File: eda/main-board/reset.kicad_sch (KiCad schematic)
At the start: 8 parts, among them U10 74HCT00, U2 NA555P

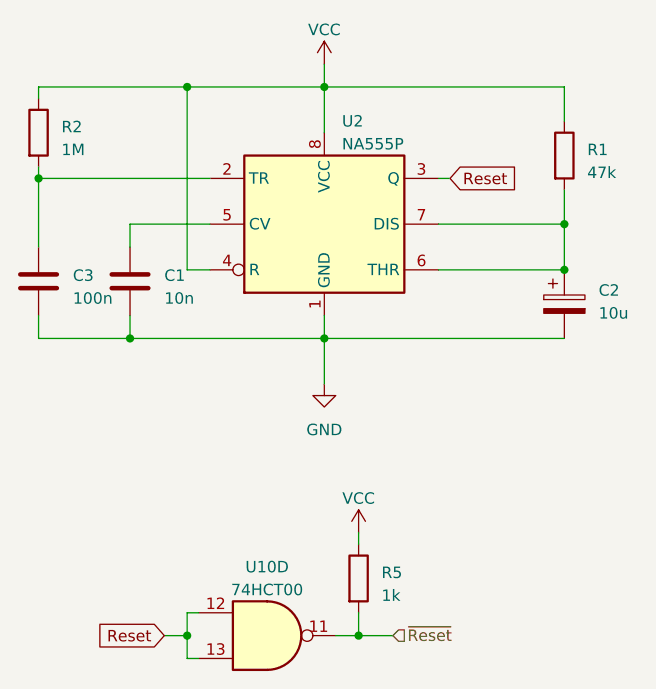
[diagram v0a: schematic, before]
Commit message: EDA work for new expansion header
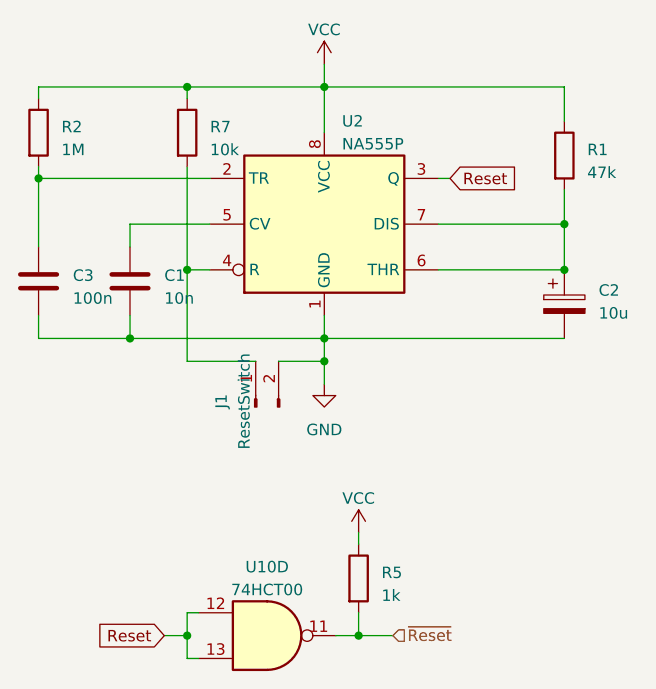
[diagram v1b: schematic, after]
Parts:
- added J1: ResetSwitch, Connector_PinHeader_2.54mm:PinHeader_1x02_P2.54mm_Vertical, symbol Connector:Conn_01x02_Pin
- added R7: 10k, Resistor_THT:R_Axial_DIN0207_L6.3mm_D2.5mm_P7.62mm_Horizontal, symbol Device:R
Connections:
- net GND: now also J1.2 (Pin_2)
- net VCC: now also R7.1; no longer U2.4 (R)
- new net: J1.1 (Pin_1), R7.2, U2.4 (R)
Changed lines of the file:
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@@
   (junction (at 129.54 69.85) (diameter 0) (color 0 0 0 0)
   )
+  (junction (at 102.87 80.01) (diameter 0) (color 0 0 0 0)
+  )
   (junction (at 102.87 77.47) (diameter 0) (color 0 0 0 0)
   )
@@
   (junction (at 87.63 110.49) (diameter 0) (color 0 0 0 0)
   )
+  (junction (at 87.63 69.85) (diameter 0) (color 0 0 0 0)
+  )
   (junction (at 71.12 59.69) (diameter 0) (color 0 0 0 0)
   )
+  (wire (pts (xy 102.87 82.55) (xy 102.87 80.01))
+    (stroke (width 0) (type default))
+  )
+  (wire (pts (xy 87.63 49.53) (xy 87.63 50.8))
+    (stroke (width 0) (type default))
+  )
+  (wire (pts (xy 81.28 77.47) (xy 102.87 77.47))
+    (stroke (width 0) (type default))
+  )
+  (wire (pts (xy 71.12 74.93) (xy 71.12 77.47))
+    (stroke (width 0) (type default))
+  )
+  (wire (pts (xy 106.68 110.49) (xy 110.49 110.49))
+    (stroke (width 0) (type default))
+  )
+  (wire (pts (xy 81.28 74.93) (xy 81.28 77.47))
+    (stroke (width 0) (type default))
+  )
+  (wire (pts (xy 71.12 77.47) (xy 81.28 77.47))
+    (stroke (width 0) (type default))
+  )
+  (wire (pts (xy 102.87 46.99) (xy 102.87 49.53))
+    (stroke (width 0) (type default))
+  )
   (wire (pts (xy 87.63 49.53) (xy 102.87 49.53))
     (stroke (width 0) (type default))
   )
-  (wire (pts (xy 102.87 82.55) (xy 102.87 77.47))
-    (stroke (width 0) (type default))
-  )
-  (wire (pts (xy 81.28 77.47) (xy 102.87 77.47))
-    (stroke (width 0) (type default))
-  )
-  (wire (pts (xy 71.12 74.93) (xy 71.12 77.47))
-    (stroke (width 0) (type default))
-  )
-  (wire (pts (xy 106.68 110.49) (xy 110.49 110.49))
-    (stroke (width 0) (type default))
-  )
-  (wire (pts (xy 81.28 74.93) (xy 81.28 77.47))
-    (stroke (width 0) (type default))
-  )
-  (wire (pts (xy 71.12 77.47) (xy 81.28 77.47))
-    (stroke (width 0) (type default))
-  )
-  (wire (pts (xy 102.87 46.99) (xy 102.87 49.53))
-    (stroke (width 0) (type default))
-  )
   (wire (pts (xy 88.9 107.95) (xy 87.63 107.95))
     (stroke (width 0) (type default))
@@
     (stroke (width 0) (type default))
   )
+  (wire (pts (xy 87.63 69.85) (xy 87.63 80.01))
+    (stroke (width 0) (type default))
+  )
   (wire (pts (xy 87.63 110.49) (xy 87.63 113.03))
     (stroke (width 0) (type default))
@@
     (stroke (width 0) (type default))
   )
+  (wire (pts (xy 87.63 58.42) (xy 87.63 69.85))
+    (stroke (width 0) (type default))
+  )
   (wire (pts (xy 129.54 64.77) (xy 115.57 64.77))
     (stroke (width 0) (type default))
@@
     (stroke (width 0) (type default))
   )
-  (wire (pts (xy 87.63 69.85) (xy 87.63 49.53))
+  (wire (pts (xy 87.63 80.01) (xy 95.25 80.01))
     (stroke (width 0) (type default))
   )
@@
     (stroke (width 0) (type default))
   )
+  (wire (pts (xy 97.79 80.01) (xy 102.87 80.01))
+    (stroke (width 0) (type default))
+  )
   (wire (pts (xy 90.17 69.85) (xy 87.63 69.85))
     (stroke (width 0) (type default))
   )
   (wire (pts (xy 81.28 67.31) (xy 81.28 64.77))
+    (stroke (width 0) (type default))
+  )
+  (wire (pts (xy 102.87 80.01) (xy 102.87 77.47))
     (stroke (width 0) (type default))
   )
@@
     )
   )
+  (symbol (lib_id "Connector:Conn_01x02_Pin") (at 95.25 85.09 90) (unit 1)
+    (in_bom yes) (on_board yes) (dnp no)
+    (property "Reference" "J1" (at 91.44 84.455 0)
+      (effects (font (size 1.27 1.27)))
+    )
+    (property "Value" "ResetSwitch" (at 93.98 84.455 0)
+      (effects (font (size 1.27 1.27)))
+    )
+    (property "Footprint" "Connector_PinHeader_2.54mm:PinHeader_1x02_P2.54mm_Vertical" (at 95.25 85.09 0)
+      (effects (font (size 1.27 1.27)) hide)
+    )
+    (property "Datasheet" "~" (at 95.25 85.09 0)
+      (effects (font (size 1.27 1.27)) hide)
+    )
+    (pin "1")
+    (pin "2")
+    (instances
+      (project "main-board"
+        (path "/2957ffac-6a43-4af7-8ab7-5cc1dbf2f2d7"
+          (reference "J1") (unit 1)
+        )
+        (path "/2957ffac-6a43-4af7-8ab7-5cc1dbf2f2d7/9790c182-812b-4e14-896c-2d1a7e725d4e"
+          (reference "J1") (unit 1)
+        )
+        (path "/2957ffac-6a43-4af7-8ab7-5cc1dbf2f2d7/9b235015-96d2-4548-9fc4-8bf7ce4b5d0e"
+          (reference "J3") (unit 1)
+        )
+      )
+    )
+  )
   (symbol (lib_id "Device:R") (at 71.12 54.61 0) (unit 1)
     (in_bom yes) (on_board yes) (dnp no) (fields_autoplaced)
@@
         )
       )
+    )
+  )
+  (symbol (lib_id "Device:R") (at 87.63 54.61 0) (unit 1)
+    (in_bom yes) (on_board yes) (dnp no) (fields_autoplaced)
+    (property "Reference" "R7" (at 90.17 53.975 0)
+      (effects (font (size 1.27 1.27)) (justify left))
+    )
+    (property "Value" "10k" (at 90.17 56.515 0)
+      (effects (font (size 1.27 1.27)) (justify left))
+    )
+    (property "Footprint" "Resistor_THT:R_Axial_DIN0207_L6.3mm_D2.5mm_P7.62mm_Horizontal" (at 85.852 54.61 90)
+      (effects (font (size 1.27 1.27)) hide)
+    )
+    (property "Datasheet" "~" (at 87.63 54.61 0)
+      (effects (font (size 1.27 1.27)) hide)
+    )
+    (pin "1")
+    (pin "2")
+    (instances
+      (project "main-board"
+        (path "/2957ffac-6a43-4af7-8ab7-5cc1dbf2f2d7/9b235015-96d2-4548-9fc4-8bf7ce4b5d0e"
+          (reference "R7") (unit 1)
+        )
+      )

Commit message: Normalize cap size
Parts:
- C3: footprint Capacitor_THT:C_Disc_D6.0mm_W2.5mm_P5.00mm -> Capacitor_THT:C_Disc_D3.8mm_W2.6mm_P2.50mm
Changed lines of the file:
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@@
       (effects (font (size 1.27 1.27)) (justify left))
     )
-    (property "Footprint" "Capacitor_THT:C_Disc_D6.0mm_W2.5mm_P5.00mm" (at 72.0852 74.93 0)
+    (property "Footprint" "Capacitor_THT:C_Disc_D3.8mm_W2.6mm_P2.50mm" (at 72.0852 74.93 0)
       (effects (font (size 1.27 1.27)) hide)
     )

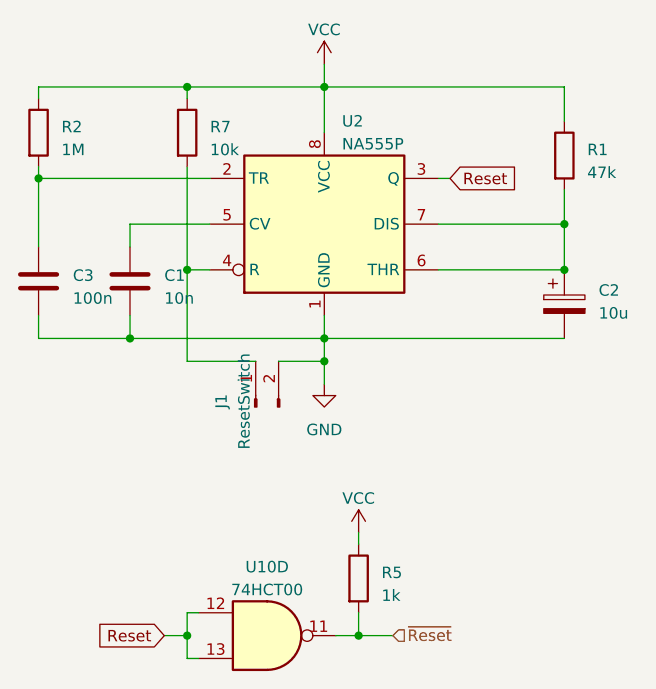
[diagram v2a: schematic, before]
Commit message: Rerouting IO card
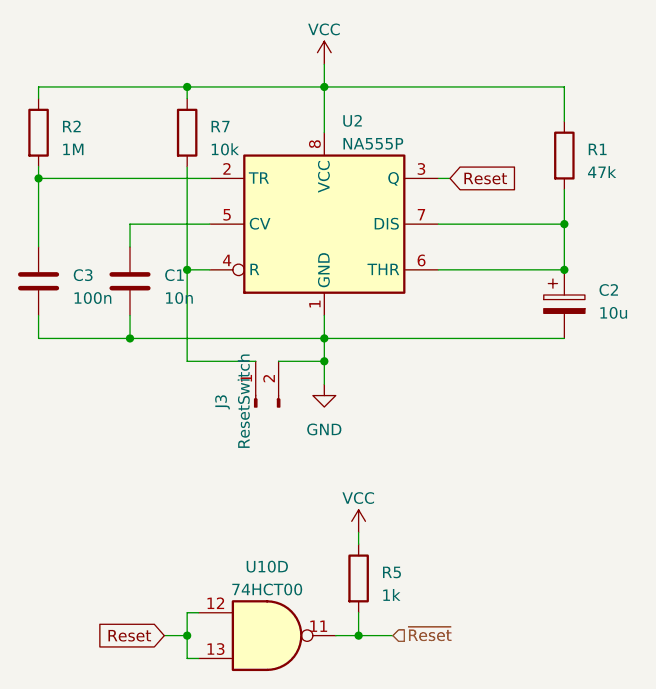
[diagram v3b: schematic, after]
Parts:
- renumbered J1 to J3
